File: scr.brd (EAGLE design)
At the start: 83.8 x 70.8 mm, 58 parts, among them IC1 MEGA8-P, IC3 LM358N, Q1 16m, T2 BT148, T3 BT148

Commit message: lagi
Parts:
- R11: value (none) -> 1k; device rcl:0207/2V -> rcl:0207/10
- moved R11 6.84 mm to (59.7, 8.89), turned to 270 degrees
- moved R8 1.27 mm to (57.1, 8.89)
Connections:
- net N$11: now also R11.1; no longer R11.2
- net VREF: now also R11.2; no longer R11.1
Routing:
- net N$12: track 5.08 -> 28.5 mm
- net N$11: track 2.54 -> 12.5 mm
- net VREF: track 27.5 -> 37.2 mm
- net TRIGER: track 93.5 -> 98.7 mm
- net N$7: track 2.54 -> 3.81 mm
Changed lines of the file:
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@@
 <element name="R26" library="rcl" package="0207/2V" value="" x="53.34" y="15.24" rot="R180"/>
 <element name="R12" library="rcl" package="0207/2V" value="" x="46.99" y="8.89" rot="R90"/>
-<element name="R11" library="rcl" package="0207/2V" value="" x="53.34" y="11.43"/>
-<element name="R8" library="rcl" package="0207/10" value="10k" x="57.15" y="10.16" rot="R90"/>
+<element name="R8" library="rcl" package="0207/10" value="10k" x="57.15" y="8.89" rot="R90"/>
 <element name="R10" library="rcl" package="0207/2V" value="" x="55.88" y="27.94" rot="R180"/>
 <element name="R2" library="rcl" package="0207/2V" value="" x="38.1" y="21.59" rot="R90"/>
 <element name="R18" library="rcl" package="0207/2V" value="" x="41.91" y="21.59" rot="R270"/>
+<element name="R11" library="rcl" package="0207/10" value="1k" x="59.69" y="8.89" rot="R270"/>
 </elements>
 <signals>
@@
 <contactref element="R26" pad="1"/>
 <wire x1="54.61" y1="15.24" x2="54.61" y2="17.78" width="1.016" layer="16"/>
-<contactref element="R11" pad="2"/>
-<wire x1="54.61" y1="11.43" x2="54.61" y2="15.24" width="0" layer="19" extent="1-1"/>
+<contactref element="R11" pad="1"/>
+<wire x1="59.69" y1="13.97" x2="59.69" y2="12.7" width="0.6096" layer="16"/>
+<wire x1="59.69" y1="12.7" x2="58.42" y2="11.43" width="0.6096" layer="16"/>
+<wire x1="58.42" y1="11.43" x2="55.88" y2="11.43" width="0.6096" layer="16"/>
+<wire x1="55.88" y1="11.43" x2="54.61" y2="12.7" width="0.6096" layer="16"/>
+<wire x1="54.61" y1="12.7" x2="54.61" y2="15.24" width="0.6096" layer="16"/>
 </signal>
 <signal name="N$12">
@@
 <contactref element="R26" pad="2"/>
 <wire x1="52.07" y1="15.24" x2="52.07" y2="17.78" width="1.016" layer="16"/>
-<wire x1="52.07" y1="17.78" x2="66.04" y2="17.78" width="0" layer="19" extent="1-1"/>
+<wire x1="52.07" y1="17.78" x2="52.07" y2="11.43" width="0.6096" layer="16"/>
+<wire x1="52.07" y1="11.43" x2="53.34" y2="10.16" width="0.6096" layer="16"/>
+<wire x1="53.34" y1="10.16" x2="59.69" y2="10.16" width="0.6096" layer="16"/>
+<wire x1="59.69" y1="10.16" x2="62.23" y2="13.97" width="0.6096" layer="16"/>
+<wire x1="62.23" y1="13.97" x2="63.5" y2="15.24" width="0.6096" layer="16"/>
+<wire x1="63.5" y1="15.24" x2="64.77" y2="15.24" width="0.6096" layer="16"/>
+<wire x1="64.77" y1="15.24" x2="66.04" y2="15.24" width="0.6096" layer="16"/>
 </signal>
 <signal name="TRIGER">
@@
 <contactref element="R12" pad="1"/>
 <contactref element="R8" pad="1"/>
-<wire x1="57.15" y1="5.08" x2="46.99" y2="7.62" width="1.016" layer="16"/>
+<wire x1="57.15" y1="3.81" x2="57.15" y2="7.62" width="1.016" layer="16"/>
+<wire x1="57.15" y1="7.62" x2="46.99" y2="7.62" width="1.016" layer="16"/>
 <wire x1="41.91" y1="49.53" x2="41.91" y2="36.83" width="1.016" layer="16"/>
 <wire x1="41.91" y1="36.83" x2="43.18" y2="35.56" width="1.016" layer="16"/>
@@
 <wire x1="69.85" y1="26.67" x2="69.85" y2="34.29" width="1.016" layer="16"/>
 <wire x1="69.85" y1="34.29" x2="66.04" y2="38.1" width="1.016" layer="16"/>
+<wire x1="57.15" y1="3.81" x2="57.15" y2="5.08" width="0.6096" layer="16"/>
 <wire x1="57.15" y1="5.08" x2="57.15" y2="7.62" width="0.6096" layer="16"/>
-<wire x1="57.15" y1="7.62" x2="63.5" y2="13.97" width="0.6096" layer="16"/>
-<wire x1="63.5" y1="13.97" x2="67.31" y2="13.97" width="0.6096" layer="16"/>
+<wire x1="57.15" y1="7.62" x2="59.69" y2="7.62" width="0.6096" layer="16"/>
+<wire x1="59.69" y1="7.62" x2="64.77" y2="13.97" width="0.6096" layer="16"/>
+<wire x1="64.77" y1="13.97" x2="67.31" y2="13.97" width="0.6096" layer="16"/>
 <wire x1="67.31" y1="13.97" x2="68.58" y2="15.24" width="0.6096" layer="16"/>
 <wire x1="68.58" y1="15.24" x2="68.58" y2="25.4" width="0.6096" layer="16"/>
@@
 <wire x1="71.12" y1="13.97" x2="71.12" y2="24.13" width="1.016" layer="16"/>
 <wire x1="71.12" y1="24.13" x2="74.93" y2="27.94" width="1.016" layer="16"/>
-<contactref element="R11" pad="1"/>
 <wire x1="74.93" y1="27.94" x2="76.2" y2="27.94" width="1.016" layer="16"/>
-<wire x1="52.07" y1="11.43" x2="66.04" y2="10.16" width="0" layer="19" extent="1-1"/>
+<contactref element="R11" pad="2"/>
+<wire x1="59.69" y1="3.81" x2="59.69" y2="5.08" width="0.6096" layer="16"/>
+<wire x1="59.69" y1="5.08" x2="64.77" y2="10.16" width="0.6096" layer="16"/>
+<wire x1="64.77" y1="10.16" x2="66.04" y2="10.16" width="0.6096" layer="16"/>
 </signal>
 <signal name="N$7">
 <contactref element="IC3" pad="3"/>
 <contactref element="R8" pad="2"/>
-<wire x1="57.15" y1="15.24" x2="57.15" y2="17.78" width="1.016" layer="16"/>
+<wire x1="57.15" y1="13.97" x2="57.15" y2="17.78" width="1.016" layer="16"/>
 </signal>
 <signal name="N$25">

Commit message: finish
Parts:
- moved R8 10.9 mm to (47.0, 12.7)
- moved R22 8.13 mm to (66.0, 50.8), turned to 270 degrees
- moved X4 3.81 mm to (72.4, 41.9)
- moved R11 3.81 mm to (59.7, 12.7), turned to 0 degrees
- moved R12 2.54 mm to (49.5, 8.89)
- moved X2 1.27 mm to (6.35, 16.5)
- moved T2 1.27 mm to (19.1, 14.0)
- moved T3 1.27 mm to (19.1, 8.89)
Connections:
- removed net N$25: R16.1, X4.3
- new net N$23: R16.1, X4.1
- net GND: now also X4.3; no longer X4.1
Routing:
- net N$25: track 39.4 -> 0.00 mm
- net N$23: track 0.00 -> 22.7 mm
- net GND: track 554.8 -> 542.7 mm, vias 2 -> 0
- net N$7: track 3.81 -> 13.8 mm
- net N$4: track 12.8 -> 22.7 mm
- net TRIGER: track 98.7 -> 90.7 mm
- net N$11: track 12.5 -> 5.08 mm
- net VREF: track 37.2 -> 30.0 mm
- net N$26: track 38.4 -> 35.3 mm
- net N$22: track 5.08 -> 7.62 mm
- net N$9: track 6.60 -> 7.87 mm
- net CTB: track 46.0 -> 44.8 mm
- net N$17: track 7.13 -> 8.40 mm
- net CTA: track 39.1 -> 40.3 mm
- net VCC: track 124.2 -> 123.3 mm
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- added copper zone on layer 16, net GND

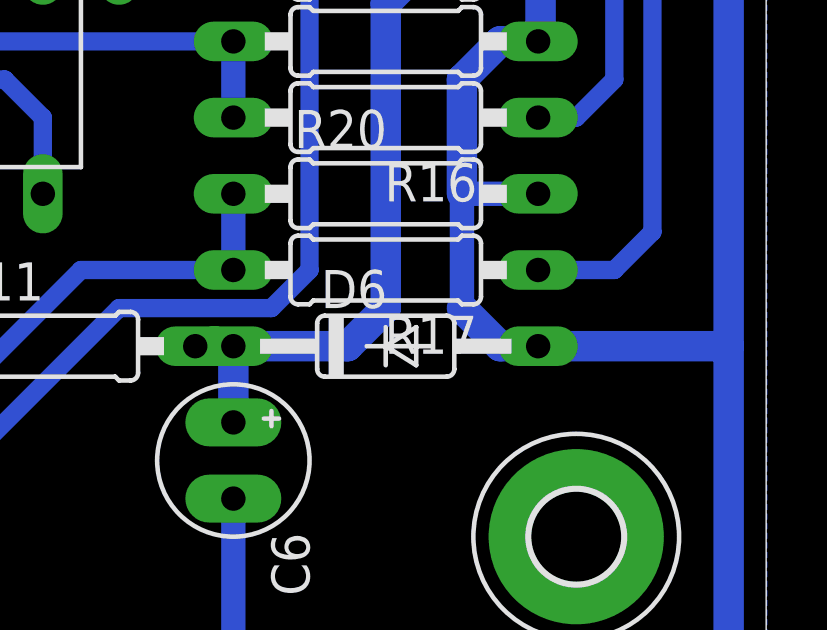
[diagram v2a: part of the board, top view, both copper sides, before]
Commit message: geser dioda
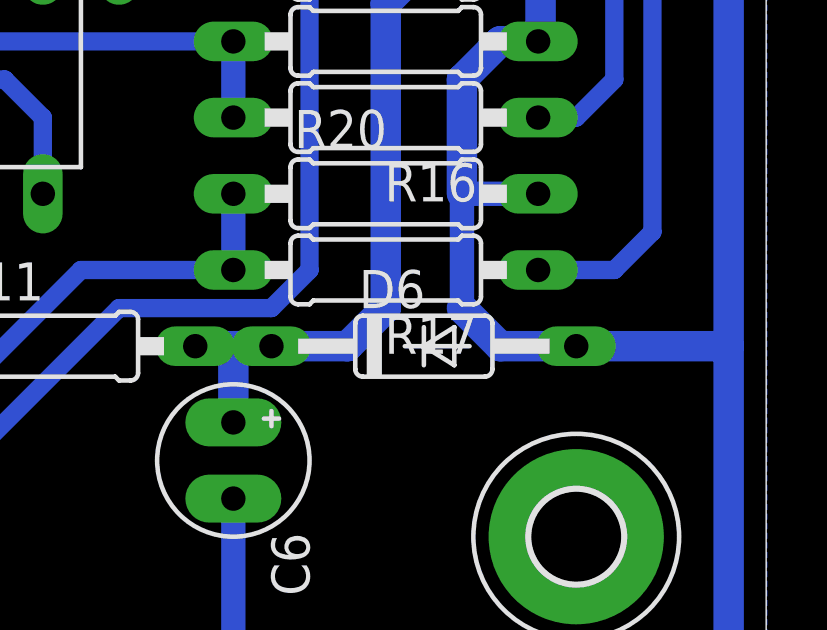
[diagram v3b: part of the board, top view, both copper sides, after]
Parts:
- moved D6 1.27 mm to (72.4, 12.7)
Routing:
- net VREF: track 30.0 -> 31.3 mm
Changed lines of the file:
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@@
 <element name="T4" library="transistor" package="TO92-CBE" value="" x="41.91" y="10.16" rot="R270"/>
 <element name="R14" library="rcl" package="0207/10" value="1k" x="49.53" y="20.32" rot="R90"/>
-<element name="D6" library="diode" package="DO35-10" value="1N4002" x="71.12" y="12.7"/>
+<element name="D6" library="diode" package="DO35-10" value="1N4002" x="72.39" y="12.7"/>
 <element name="R15" library="rcl" package="0207/10" value="10k" x="71.12" y="30.48" rot="R180"/>
 <element name="R16" library="rcl" package="0207/10" value="1k" x="71.12" y="20.32" rot="R180"/>
@@
 <wire x1="66.04" y1="7.62" x2="66.04" y2="1.27" width="0.8128" layer="16"/>
 <wire x1="73.66" y1="17.78" x2="73.66" y2="13.97" width="0.8128" layer="16"/>
-<wire x1="76.2" y1="12.7" x2="82.55" y2="12.7" width="1.016" layer="16"/>
-<wire x1="76.2" y1="12.7" x2="74.93" y2="12.7" width="1.016" layer="16"/>
+<wire x1="77.47" y1="12.7" x2="82.55" y2="12.7" width="1.016" layer="16"/>
+<wire x1="77.47" y1="12.7" x2="74.93" y2="12.7" width="1.016" layer="16"/>
 <wire x1="74.93" y1="12.7" x2="73.66" y2="13.97" width="1.016" layer="16"/>
 <wire x1="76.28" y1="22.94" x2="76.2" y2="22.86" width="1.016" layer="16"/>
@@
 <contactref element="R11" pad="2"/>
 <wire x1="64.77" y1="10.16" x2="66.04" y2="10.16" width="0.6096" layer="16"/>
-<wire x1="64.77" y1="12.7" x2="66.04" y2="12.7" width="1.016" layer="16"/>
-<wire x1="66.04" y1="12.7" x2="69.85" y2="12.7" width="1.016" layer="16"/>
+<wire x1="64.77" y1="12.7" x2="67.31" y2="12.7" width="1.016" layer="16"/>
+<wire x1="67.31" y1="12.7" x2="69.85" y2="12.7" width="1.016" layer="16"/>
 <wire x1="66.04" y1="10.16" x2="66.04" y2="12.7" width="1.016" layer="16"/>
+<wire x1="66.04" y1="12.7" x2="67.31" y2="12.7" width="1.016" layer="16"/>
 </signal>
 <signal name="N$7">
